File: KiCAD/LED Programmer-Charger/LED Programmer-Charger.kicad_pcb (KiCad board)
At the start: 2 copper layers, 42 x 26 mm, 17 parts, among them J1 USB_B_Micro, J2 UPDI socket, SW2 SW_SPDT, U1 CH340C, U2 LTC4126EV-10_TRMPBF

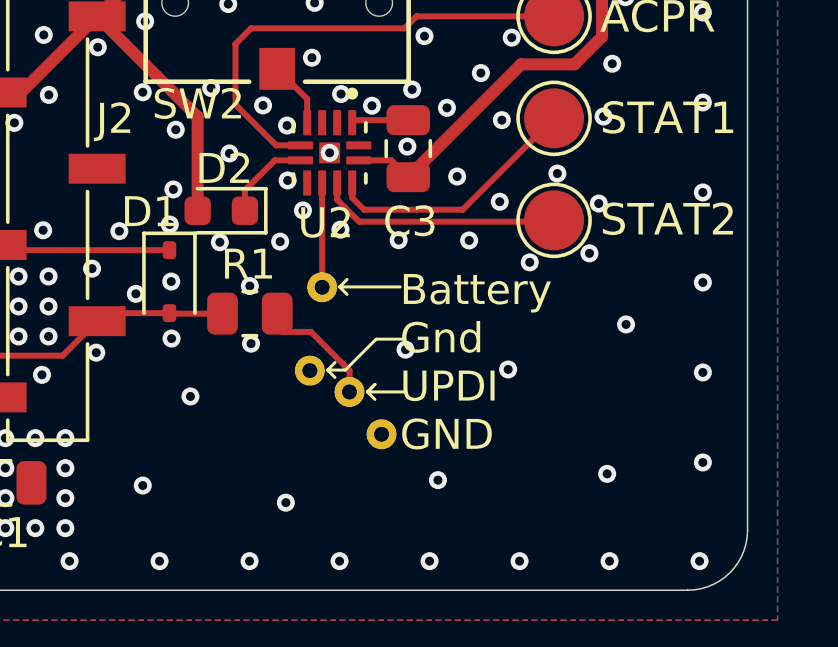
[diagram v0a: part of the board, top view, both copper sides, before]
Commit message: Build CAD files of assembly
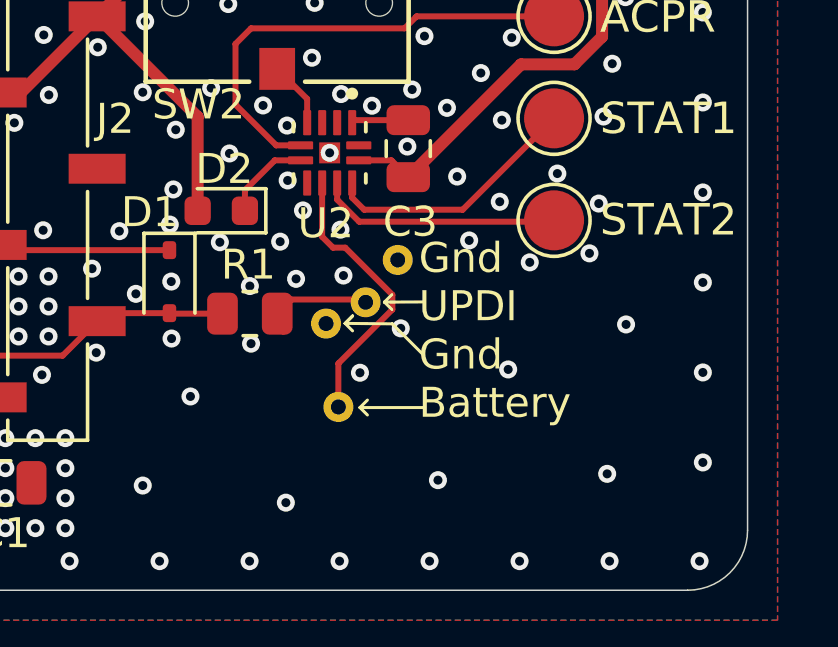
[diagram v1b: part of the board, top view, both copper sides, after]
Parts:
- TP4: moved to F.Cu
- moved TP4 1.66 mm to (115.0, 79.1)
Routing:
- net +Vbat: track 3.48 -> 9.42 mm
- net GND: vias 180 -> 182
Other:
- board text added: "Gnd UPDI Gnd Battery"
- board text removed: "Battery Gnd UPDI GND"

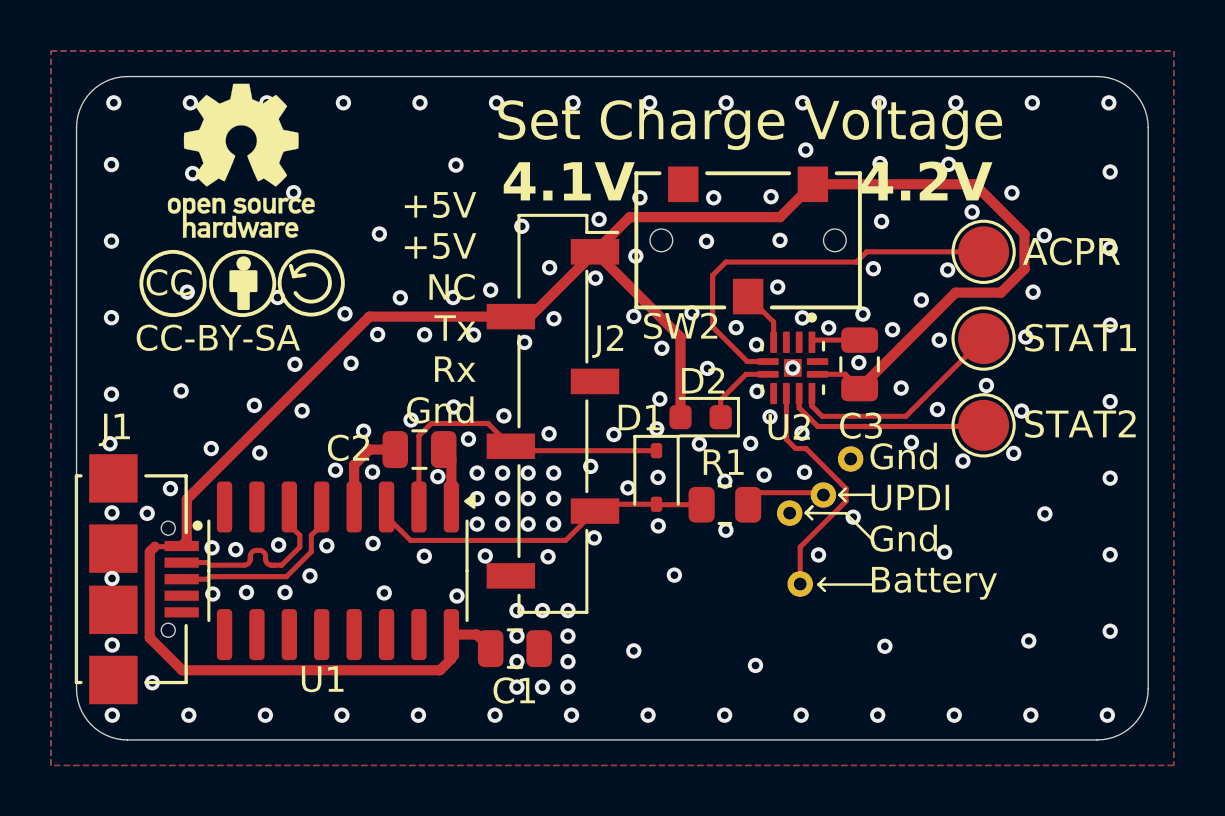
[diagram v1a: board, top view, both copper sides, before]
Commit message: Remove status pads for charger as DC-DC converter is required
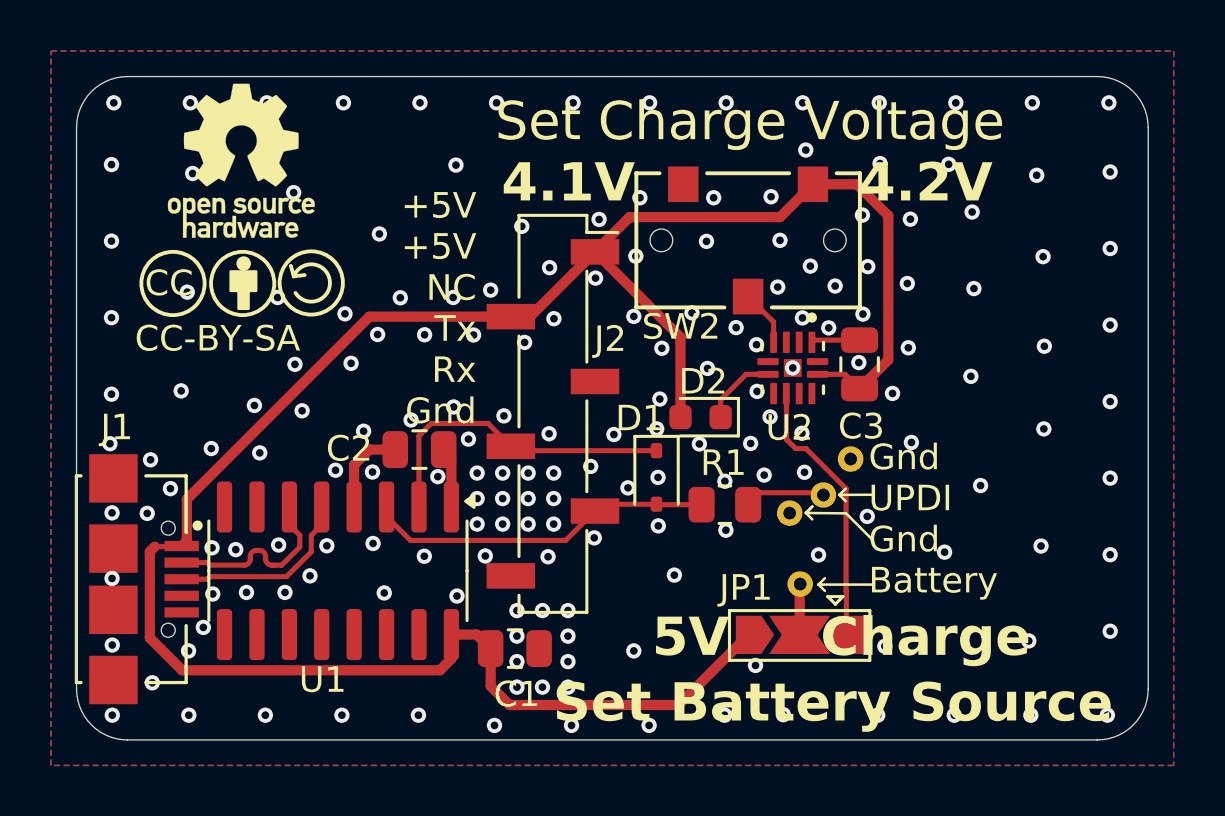
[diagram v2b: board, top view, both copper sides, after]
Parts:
- removed TP0, TP1, TP2: TestPoint, TestPoint:TestPoint_Pad_D2.0mm
- added JP1: Jumper_3_Open, Jumper:SolderJumper-3_P2.0mm_Open_TrianglePad1.0x1.5mm, F.Cu at (115.3, 83.9)
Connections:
- TP4 pad 3: +Vbat -> Net-(JP1-C)
- U2 pad 10: Net-(U2-STAT1) -> unconnected-(U2-STAT1-Pad10)
- U2 pad 5: Net-(U2-ACPR) -> unconnected-(U2-ACPR-Pad5)
- U2 pad 9: Net-(U2-STAT2) -> unconnected-(U2-STAT2-Pad9)
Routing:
- net Net-(U2-ACPR): track 15.8 -> 0.00 mm
- net Net-(U2-STAT1): track 8.65 -> 0.00 mm
- net Net-(U2-STAT2): track 8.11 -> 0.00 mm
- net +5V: track 80.1 -> 85.0 mm
- net Net-(JP1-C): track 0.00 -> 2.00 mm
- net +Vbat: track 9.42 -> 10.7 mm
- net GND: vias 182 -> 184
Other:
- board text added: "5V Charge"
- board text added: "Set Battery Source"
- board text removed: "ACPR STAT1 STAT2"
